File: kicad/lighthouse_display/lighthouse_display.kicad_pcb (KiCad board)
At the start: 2 copper layers, 0 parts

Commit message: sch: all leds connected, also set all footprints
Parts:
- added C1: 100nF, Capacitor_SMD:C_0603_1608Metric_Pad1.08x0.95mm_HandSolder, F.Cu at (237.0, 76.7)
- added C11: 1uF, Capacitor_SMD:C_0805_2012Metric_Pad1.18x1.45mm_HandSolder, F.Cu at (250.3, 89.0)
- added C2: 10uF, Capacitor_SMD:C_0805_2012Metric_Pad1.18x1.45mm_HandSolder, F.Cu at (250.3, 77.0)
- added C3: 470nF, Capacitor_SMD:C_0603_1608Metric_Pad1.08x0.95mm_HandSolder, F.Cu at (237.0, 79.2)
- added C4: 1uF, Capacitor_SMD:C_0805_2012Metric_Pad1.18x1.45mm_HandSolder, F.Cu at (250.3, 80.0)
- added C5: 10uF, Capacitor_SMD:C_0805_2012Metric_Pad1.18x1.45mm_HandSolder, F.Cu at (250.3, 83.0)
- added C6: 100nF, Capacitor_SMD:C_0603_1608Metric_Pad1.08x0.95mm_HandSolder, F.Cu at (237.0, 81.7)
- added C7: 10uF, Capacitor_SMD:C_0805_2012Metric_Pad1.18x1.45mm_HandSolder, F.Cu at (250.3, 86.0)
- added C8: 100nF, Capacitor_SMD:C_0603_1608Metric_Pad1.08x0.95mm_HandSolder, F.Cu at (237.0, 84.2)
- added D1: 1206MIL, LED_SMD:LED_1206_3216Metric_Pad1.42x1.75mm_HandSolder, F.Cu at (189.7, 77.1)
- added D10: 1206MIL, LED_SMD:LED_1206_3216Metric_Pad1.42x1.75mm_HandSolder, F.Cu at (189.7, 107.7)
- added D100: PMEG4010CEJ, Diode_SMD:D_SOD-323F, F.Cu at (254.8, 82.2)
- added D11: 1206MIL, LED_SMD:LED_1206_3216Metric_Pad1.42x1.75mm_HandSolder, F.Cu at (189.7, 111.1)
- added D12: 1206MIL, LED_SMD:LED_1206_3216Metric_Pad1.42x1.75mm_HandSolder, F.Cu at (189.7, 114.5)
- added D13: 1206MIL, LED_SMD:LED_1206_3216Metric_Pad1.42x1.75mm_HandSolder, F.Cu at (189.7, 117.8)
- added D14: 1206MIL, LED_SMD:LED_1206_3216Metric_Pad1.42x1.75mm_HandSolder, F.Cu at (189.7, 121.2)
- added D15: 1206MIL, LED_SMD:LED_1206_3216Metric_Pad1.42x1.75mm_HandSolder, F.Cu at (189.7, 124.6)
- added D16: 1206MIL, LED_SMD:LED_1206_3216Metric_Pad1.42x1.75mm_HandSolder, F.Cu at (195.7, 77.2)
- added D17: 1206MIL, LED_SMD:LED_1206_3216Metric_Pad1.42x1.75mm_HandSolder, F.Cu at (195.7, 80.5)
- added D18: 1206MIL, LED_SMD:LED_1206_3216Metric_Pad1.42x1.75mm_HandSolder, F.Cu at (195.7, 83.9)
- added D19: 1206MIL, LED_SMD:LED_1206_3216Metric_Pad1.42x1.75mm_HandSolder, F.Cu at (195.7, 87.3)
- added D2: 1206MIL, LED_SMD:LED_1206_3216Metric_Pad1.42x1.75mm_HandSolder, F.Cu at (189.7, 80.5)
- added D20: 1206MIL, LED_SMD:LED_1206_3216Metric_Pad1.42x1.75mm_HandSolder, F.Cu at (195.7, 90.7)
- added D21: 1206MIL, LED_SMD:LED_1206_3216Metric_Pad1.42x1.75mm_HandSolder, F.Cu at (195.7, 94.1)
- added D22: 1206MIL, LED_SMD:LED_1206_3216Metric_Pad1.42x1.75mm_HandSolder, F.Cu at (195.7, 97.5)
- added D23: 1206MIL, LED_SMD:LED_1206_3216Metric_Pad1.42x1.75mm_HandSolder, F.Cu at (195.7, 100.9)
- added D24: 1206MIL, LED_SMD:LED_1206_3216Metric_Pad1.42x1.75mm_HandSolder, F.Cu at (195.7, 104.3)
- added D25: 1206MIL, LED_SMD:LED_1206_3216Metric_Pad1.42x1.75mm_HandSolder, F.Cu at (195.7, 107.7)
- added D26: 1206MIL, LED_SMD:LED_1206_3216Metric_Pad1.42x1.75mm_HandSolder, F.Cu at (195.7, 111.1)
- added D27: 1206MIL, LED_SMD:LED_1206_3216Metric_Pad1.42x1.75mm_HandSolder, F.Cu at (195.7, 114.5)
- added D28: 1206MIL, LED_SMD:LED_1206_3216Metric_Pad1.42x1.75mm_HandSolder, F.Cu at (195.7, 117.8)
- added D29: 1206MIL, LED_SMD:LED_1206_3216Metric_Pad1.42x1.75mm_HandSolder, F.Cu at (195.7, 121.2)
- added D3: 1206MIL, LED_SMD:LED_1206_3216Metric_Pad1.42x1.75mm_HandSolder, F.Cu at (189.7, 83.9)
- added D30: 1206MIL, LED_SMD:LED_1206_3216Metric_Pad1.42x1.75mm_HandSolder, F.Cu at (195.7, 124.6)
- added D31: 1206MIL, LED_SMD:LED_1206_3216Metric_Pad1.42x1.75mm_HandSolder, F.Cu at (201.7, 77.2)
- added D32: 1206MIL, LED_SMD:LED_1206_3216Metric_Pad1.42x1.75mm_HandSolder, F.Cu at (201.7, 80.5)
- added D33: 1206MIL, LED_SMD:LED_1206_3216Metric_Pad1.42x1.75mm_HandSolder, F.Cu at (201.7, 83.9)
- added D34: 1206MIL, LED_SMD:LED_1206_3216Metric_Pad1.42x1.75mm_HandSolder, F.Cu at (201.7, 87.3)
- added D35: 1206MIL, LED_SMD:LED_1206_3216Metric_Pad1.42x1.75mm_HandSolder, F.Cu at (201.7, 90.7)
- added D36: 1206MIL, LED_SMD:LED_1206_3216Metric_Pad1.42x1.75mm_HandSolder, F.Cu at (201.7, 94.1)
- added D37: 1206MIL, LED_SMD:LED_1206_3216Metric_Pad1.42x1.75mm_HandSolder, F.Cu at (201.7, 97.5)
- added D38: 1206MIL, LED_SMD:LED_1206_3216Metric_Pad1.42x1.75mm_HandSolder, F.Cu at (201.7, 100.9)
- added D39: 1206MIL, LED_SMD:LED_1206_3216Metric_Pad1.42x1.75mm_HandSolder, F.Cu at (201.7, 104.3)
- added D4: 1206MIL, LED_SMD:LED_1206_3216Metric_Pad1.42x1.75mm_HandSolder, F.Cu at (189.7, 87.3)
- added D40: 1206MIL, LED_SMD:LED_1206_3216Metric_Pad1.42x1.75mm_HandSolder, F.Cu at (201.7, 107.7)
- added D41: 1206MIL, LED_SMD:LED_1206_3216Metric_Pad1.42x1.75mm_HandSolder, F.Cu at (201.7, 111.1)
- added D42: 1206MIL, LED_SMD:LED_1206_3216Metric_Pad1.42x1.75mm_HandSolder, F.Cu at (201.7, 114.5)
- added D43: 1206MIL, LED_SMD:LED_1206_3216Metric_Pad1.42x1.75mm_HandSolder, F.Cu at (201.7, 117.8)
- added D44: 1206MIL, LED_SMD:LED_1206_3216Metric_Pad1.42x1.75mm_HandSolder, F.Cu at (201.7, 121.2)
- added D45: 1206MIL, LED_SMD:LED_1206_3216Metric_Pad1.42x1.75mm_HandSolder, F.Cu at (201.7, 124.6)
- added D46: 1206MIL, LED_SMD:LED_1206_3216Metric_Pad1.42x1.75mm_HandSolder, F.Cu at (207.7, 77.2)
- added D47: 1206MIL, LED_SMD:LED_1206_3216Metric_Pad1.42x1.75mm_HandSolder, F.Cu at (207.7, 80.5)
- added D48: 1206MIL, LED_SMD:LED_1206_3216Metric_Pad1.42x1.75mm_HandSolder, F.Cu at (207.7, 83.9)
- added D49: 1206MIL, LED_SMD:LED_1206_3216Metric_Pad1.42x1.75mm_HandSolder, F.Cu at (207.7, 87.3)
- added D5: 1206MIL, LED_SMD:LED_1206_3216Metric_Pad1.42x1.75mm_HandSolder, F.Cu at (189.7, 90.7)
- added D50: 1206MIL, LED_SMD:LED_1206_3216Metric_Pad1.42x1.75mm_HandSolder, F.Cu at (207.7, 90.7)
- added D51: 1206MIL, LED_SMD:LED_1206_3216Metric_Pad1.42x1.75mm_HandSolder, F.Cu at (207.7, 94.1)
- added D52: 1206MIL, LED_SMD:LED_1206_3216Metric_Pad1.42x1.75mm_HandSolder, F.Cu at (207.7, 97.5)
- added D53: 1206MIL, LED_SMD:LED_1206_3216Metric_Pad1.42x1.75mm_HandSolder, F.Cu at (207.7, 100.9)
- added D54: 1206MIL, LED_SMD:LED_1206_3216Metric_Pad1.42x1.75mm_HandSolder, F.Cu at (207.7, 104.3)
- added D55: 1206MIL, LED_SMD:LED_1206_3216Metric_Pad1.42x1.75mm_HandSolder, F.Cu at (207.7, 107.7)
- added D56: 1206MIL, LED_SMD:LED_1206_3216Metric_Pad1.42x1.75mm_HandSolder, F.Cu at (207.7, 111.1)
- added D57: 1206MIL, LED_SMD:LED_1206_3216Metric_Pad1.42x1.75mm_HandSolder, F.Cu at (207.7, 114.5)
- added D58: 1206MIL, LED_SMD:LED_1206_3216Metric_Pad1.42x1.75mm_HandSolder, F.Cu at (207.7, 117.8)
- added D59: 1206MIL, LED_SMD:LED_1206_3216Metric_Pad1.42x1.75mm_HandSolder, F.Cu at (207.7, 121.2)
- added D6: 1206MIL, LED_SMD:LED_1206_3216Metric_Pad1.42x1.75mm_HandSolder, F.Cu at (189.7, 94.1)
- added D60: 1206MIL, LED_SMD:LED_1206_3216Metric_Pad1.42x1.75mm_HandSolder, F.Cu at (207.7, 124.6)
- added D61: 1206MIL, LED_SMD:LED_1206_3216Metric_Pad1.42x1.75mm_HandSolder, F.Cu at (213.7, 77.2)
- added D62: 1206MIL, LED_SMD:LED_1206_3216Metric_Pad1.42x1.75mm_HandSolder, F.Cu at (213.7, 80.5)
- added D63: 1206MIL, LED_SMD:LED_1206_3216Metric_Pad1.42x1.75mm_HandSolder, F.Cu at (213.7, 83.9)
- added D64: 1206MIL, LED_SMD:LED_1206_3216Metric_Pad1.42x1.75mm_HandSolder, F.Cu at (213.7, 87.3)
- added D65: 1206MIL, LED_SMD:LED_1206_3216Metric_Pad1.42x1.75mm_HandSolder, F.Cu at (213.7, 90.7)
- added D66: 1206MIL, LED_SMD:LED_1206_3216Metric_Pad1.42x1.75mm_HandSolder, F.Cu at (213.7, 94.1)
- added D67: 1206MIL, LED_SMD:LED_1206_3216Metric_Pad1.42x1.75mm_HandSolder, F.Cu at (213.7, 97.5)
- added D68: 1206MIL, LED_SMD:LED_1206_3216Metric_Pad1.42x1.75mm_HandSolder, F.Cu at (213.7, 100.9)
- added D69: 1206MIL, LED_SMD:LED_1206_3216Metric_Pad1.42x1.75mm_HandSolder, F.Cu at (213.7, 104.3)
- added D7: 1206MIL, LED_SMD:LED_1206_3216Metric_Pad1.42x1.75mm_HandSolder, F.Cu at (189.7, 97.5)
- added D70: 1206MIL, LED_SMD:LED_1206_3216Metric_Pad1.42x1.75mm_HandSolder, F.Cu at (213.7, 107.7)
- added D71: 1206MIL, LED_SMD:LED_1206_3216Metric_Pad1.42x1.75mm_HandSolder, F.Cu at (213.7, 111.1)
- added D72: 1206MIL, LED_SMD:LED_1206_3216Metric_Pad1.42x1.75mm_HandSolder, F.Cu at (213.7, 114.5)
- added D73: 1206MIL, LED_SMD:LED_1206_3216Metric_Pad1.42x1.75mm_HandSolder, F.Cu at (213.7, 117.8)
- added D74: 1206MIL, LED_SMD:LED_1206_3216Metric_Pad1.42x1.75mm_HandSolder, F.Cu at (213.7, 121.2)
- added D75: 1206MIL, LED_SMD:LED_1206_3216Metric_Pad1.42x1.75mm_HandSolder, F.Cu at (213.7, 124.6)
- added D76: 1206MIL, LED_SMD:LED_1206_3216Metric_Pad1.42x1.75mm_HandSolder, F.Cu at (219.7, 77.2)
- added D77: 1206MIL, LED_SMD:LED_1206_3216Metric_Pad1.42x1.75mm_HandSolder, F.Cu at (219.7, 80.5)
- added D78: 1206MIL, LED_SMD:LED_1206_3216Metric_Pad1.42x1.75mm_HandSolder, F.Cu at (219.7, 83.9)
- added D79: 1206MIL, LED_SMD:LED_1206_3216Metric_Pad1.42x1.75mm_HandSolder, F.Cu at (219.7, 87.3)
- added D8: 1206MIL, LED_SMD:LED_1206_3216Metric_Pad1.42x1.75mm_HandSolder, F.Cu at (189.7, 100.9)
- added D80: 1206MIL, LED_SMD:LED_1206_3216Metric_Pad1.42x1.75mm_HandSolder, F.Cu at (219.7, 90.7)
- added D81: 1206MIL, LED_SMD:LED_1206_3216Metric_Pad1.42x1.75mm_HandSolder, F.Cu at (219.7, 94.1)
- added D82: 1206MIL, LED_SMD:LED_1206_3216Metric_Pad1.42x1.75mm_HandSolder, F.Cu at (219.7, 97.5)
- added D83: 1206MIL, LED_SMD:LED_1206_3216Metric_Pad1.42x1.75mm_HandSolder, F.Cu at (219.7, 100.9)
- added D84: 1206MIL, LED_SMD:LED_1206_3216Metric_Pad1.42x1.75mm_HandSolder, F.Cu at (219.7, 104.3)
- added D85: 1206MIL, LED_SMD:LED_1206_3216Metric_Pad1.42x1.75mm_HandSolder, F.Cu at (219.7, 107.7)
- added D86: 1206MIL, LED_SMD:LED_1206_3216Metric_Pad1.42x1.75mm_HandSolder, F.Cu at (219.7, 111.1)
- added D87: 1206MIL, LED_SMD:LED_1206_3216Metric_Pad1.42x1.75mm_HandSolder, F.Cu at (219.7, 114.5)
- added D88: 1206MIL, LED_SMD:LED_1206_3216Metric_Pad1.42x1.75mm_HandSolder, F.Cu at (219.7, 117.8)
- added D89: 1206MIL, LED_SMD:LED_1206_3216Metric_Pad1.42x1.75mm_HandSolder, F.Cu at (219.7, 121.2)
- added D9: 1206MIL, LED_SMD:LED_1206_3216Metric_Pad1.42x1.75mm_HandSolder, F.Cu at (189.7, 104.3)
- added D90: 1206MIL, LED_SMD:LED_1206_3216Metric_Pad1.42x1.75mm_HandSolder, F.Cu at (219.7, 124.6)
- added D91: 1206MIL, LED_SMD:LED_1206_3216Metric_Pad1.42x1.75mm_HandSolder, F.Cu at (225.7, 77.2)
- added D92: 1206MIL, LED_SMD:LED_1206_3216Metric_Pad1.42x1.75mm_HandSolder, F.Cu at (225.7, 80.5)
- added D93: 1206MIL, LED_SMD:LED_1206_3216Metric_Pad1.42x1.75mm_HandSolder, F.Cu at (225.7, 83.9)
- added D94: 1206MIL, LED_SMD:LED_1206_3216Metric_Pad1.42x1.75mm_HandSolder, F.Cu at (225.7, 87.3)
- added D95: 1206MIL, LED_SMD:LED_1206_3216Metric_Pad1.42x1.75mm_HandSolder, F.Cu at (225.7, 90.7)
- added D96: 1206MIL, LED_SMD:LED_1206_3216Metric_Pad1.42x1.75mm_HandSolder, F.Cu at (225.7, 94.1)
- added D97: 1206MIL, LED_SMD:LED_1206_3216Metric_Pad1.42x1.75mm_HandSolder, F.Cu at (225.7, 97.5)
- added D98: 1206MIL, LED_SMD:LED_1206_3216Metric_Pad1.42x1.75mm_HandSolder, F.Cu at (225.7, 100.9)
- added D99: 1206MIL, LED_SMD:LED_1206_3216Metric_Pad1.42x1.75mm_HandSolder, F.Cu at (225.7, 104.3)
- added J1: Conn_01x12_Pin, Connector_PinHeader_1.27mm:PinHeader_1x12_P1.27mm_Vertical, F.Cu at (232.7, 77.1)
- added L1: 4.7uH, Inductor_SMD:L_Taiyo-Yuden_NR-60xx_HandSoldering, F.Cu at (250.1, 94.3)
- added R1: 1M3, Resistor_SMD:R_0603_1608Metric_Pad0.98x0.95mm_HandSolder, F.Cu at (237.0, 86.8)
- added R10: 1M, Resistor_SMD:R_0603_1608Metric_Pad0.98x0.95mm_HandSolder, F.Cu at (245.7, 79.2)
- added R11: 1M, Resistor_SMD:R_0603_1608Metric_Pad0.98x0.95mm_HandSolder, F.Cu at (245.7, 81.7)
- added R12: 20k, Resistor_SMD:R_0603_1608Metric_Pad0.98x0.95mm_HandSolder, F.Cu at (245.7, 84.2)
- added R2: 51k, Resistor_SMD:R_0603_1608Metric_Pad0.98x0.95mm_HandSolder, F.Cu at (237.0, 89.3)
- added R3: 1M, Resistor_SMD:R_0603_1608Metric_Pad0.98x0.95mm_HandSolder, F.Cu at (241.3, 76.7)
- added R4: 83k3, Resistor_SMD:R_0603_1608Metric_Pad0.98x0.95mm_HandSolder, F.Cu at (241.3, 79.2)
- added R5: 1M, Resistor_SMD:R_0603_1608Metric_Pad0.98x0.95mm_HandSolder, F.Cu at (241.3, 81.7)
- added R6: 4k7, Resistor_SMD:R_0603_1608Metric_Pad0.98x0.95mm_HandSolder, F.Cu at (241.3, 84.2)
- added R7: 4k7, Resistor_SMD:R_0603_1608Metric_Pad0.98x0.95mm_HandSolder, F.Cu at (241.3, 86.8)
- added R8: 1M, Resistor_SMD:R_0603_1608Metric_Pad0.98x0.95mm_HandSolder, F.Cu at (241.3, 89.3)
- added R9: 1M, Resistor_SMD:R_0603_1608Metric_Pad0.98x0.95mm_HandSolder, F.Cu at (245.7, 76.7)
- added U1: IS31FL3731-SA, Package_SO:SSOP-28_5.3x10.2mm_P0.65mm, F.Cu at (240.1, 96.5)
- added U2: TPS61176RTER, Package_DFN_QFN:Texas_RTE0016D_WQFN-16-1EP_3x3mm_P0.5mm_EP0.8x0.8mm, F.Cu at (255.3, 78.1)

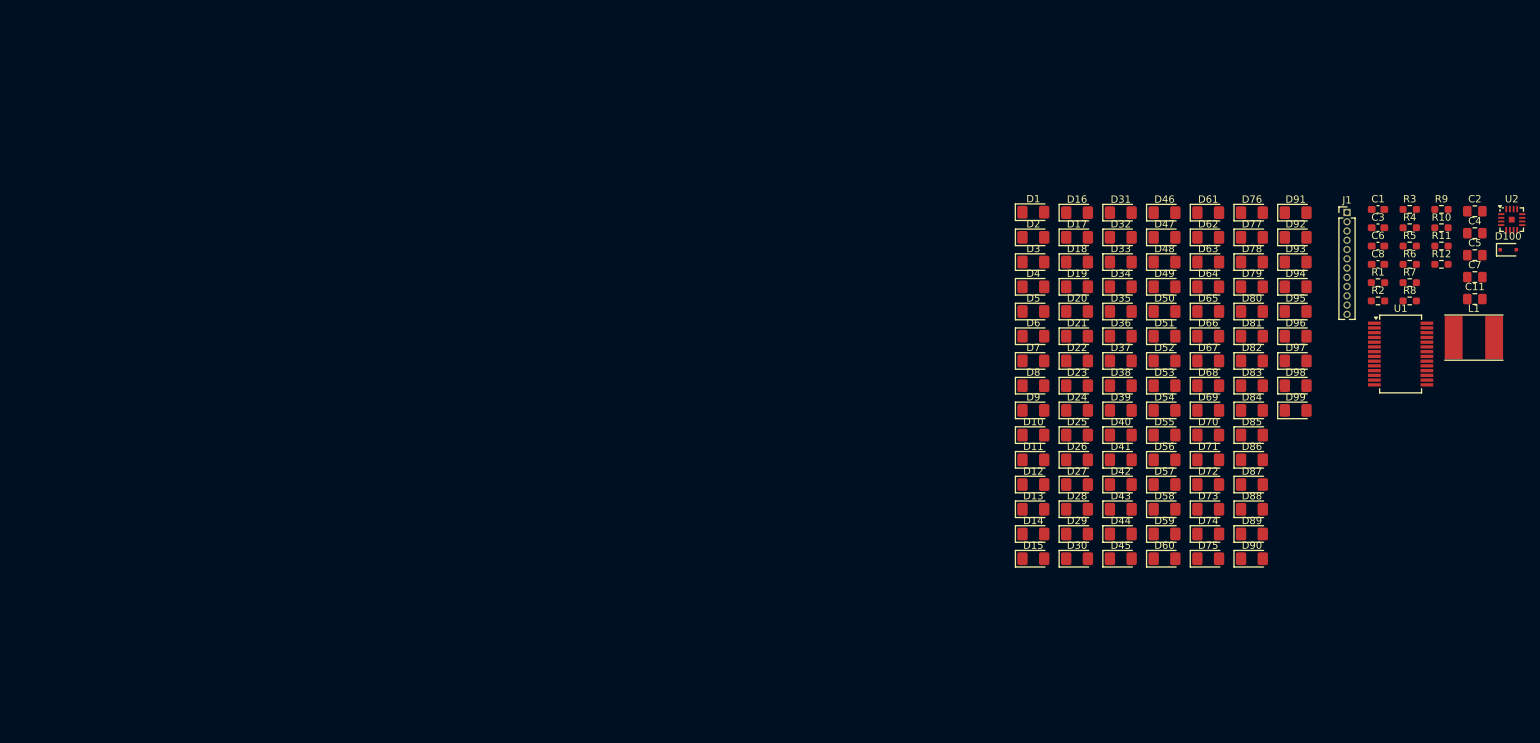
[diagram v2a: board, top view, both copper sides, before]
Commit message: hw display placed red and white leds
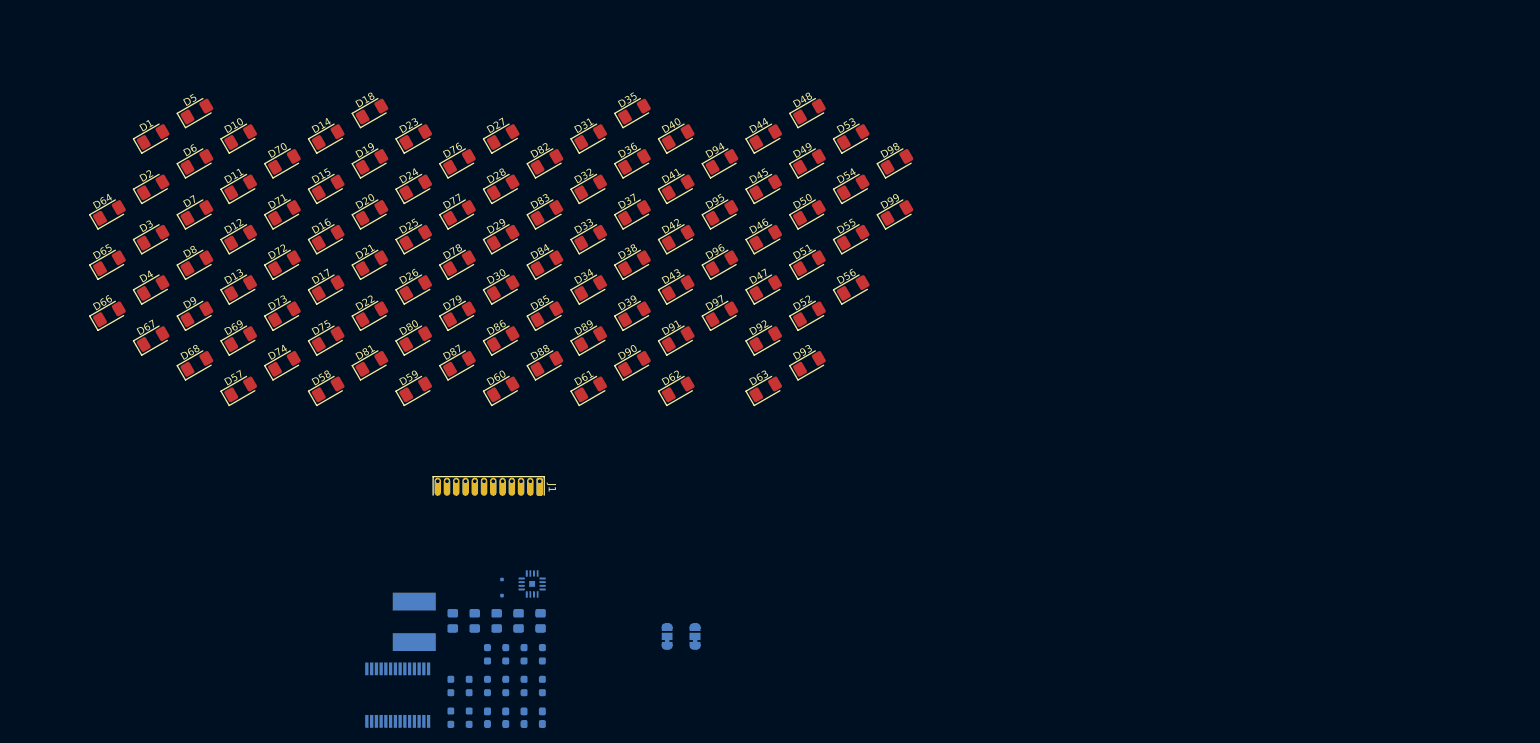
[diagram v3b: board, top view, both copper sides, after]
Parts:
- added JP1: Jumper_3_Bridged12, Jumper:SolderJumper-3_P1.3mm_Bridged12_RoundedPad1.0x1.5mm, B.Cu at (143.3, 135.3)
- added JP2: Jumper_3_Bridged12, Jumper:SolderJumper-3_P1.3mm_Bridged12_RoundedPad1.0x1.5mm, B.Cu at (139.5, 135.3)
- C1, C11, C2, C3, C4, C5, C6, C7, C8, D100, L1, R1, R10, R11, R12, R2, R3, R4, R5, R6, R7, R8, R9, U1, U2: moved to B.Cu
- J1: footprint Connector_PinHeader_1.27mm:PinHeader_1x12_P1.27mm_Vertical -> lighthouse:con_1x12_1.27mm_long_pads
- moved D64 151.0 mm to (63.0, 77.2), turned to 30 degrees
- moved D65 150.8 mm to (63.0, 84.1), turned to 30 degrees
- moved D66 150.7 mm to (63.0, 91.1), turned to 30 degrees
- moved L1 150.5 mm to (104.8, 133.3), turned to 90 degrees
- moved C11 146.9 mm to (110.1, 133.1), turned to 90 degrees
- moved D100 145.5 mm to (116.8, 128.6), turned to 90 degrees
- moved U1 145.3 mm to (102.5, 143.3), turned to 90 degrees
- moved C7 145.0 mm to (113.1, 133.1), turned to 90 degrees
- moved D67 144.7 mm to (69.0, 94.5), turned to 30 degrees
- moved U2 143.3 mm to (121.0, 128.1), turned to 90 degrees
- moved C5 143.2 mm to (116.1, 133.1), turned to 90 degrees
- moved R8 141.7 mm to (109.8, 142.1), turned to 90 degrees
- moved C4 141.5 mm to (119.1, 133.1), turned to 90 degrees
- moved R12 141.3 mm to (114.8, 137.7), turned to 90 degrees
- moved R7 140.3 mm to (112.3, 142.1), turned to 90 degrees
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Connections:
- C1 pad 1: +BATT -> +12V
- C11 pad 1: +3.3V -> Net-(JP1-C)
- C2 pad 1: +BATT -> +12V
- C7 pad 1: +BATT -> Net-(JP2-C)
- C8 pad 1: +BATT -> Net-(JP2-C)
- J1 pad 1: +BATT -> +12V
- J1 pad 12: GND -> unconnected-(J1-Pin_12-Pad12)
- J1 pad 2: GND -> +5V
- L1 pad 1: +BATT -> +12V
- U1 pad 2: +BATT -> Net-(JP2-C)
- U2 pad 15: +3.3V -> Net-(JP1-C)

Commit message: places both led drivers, started routing
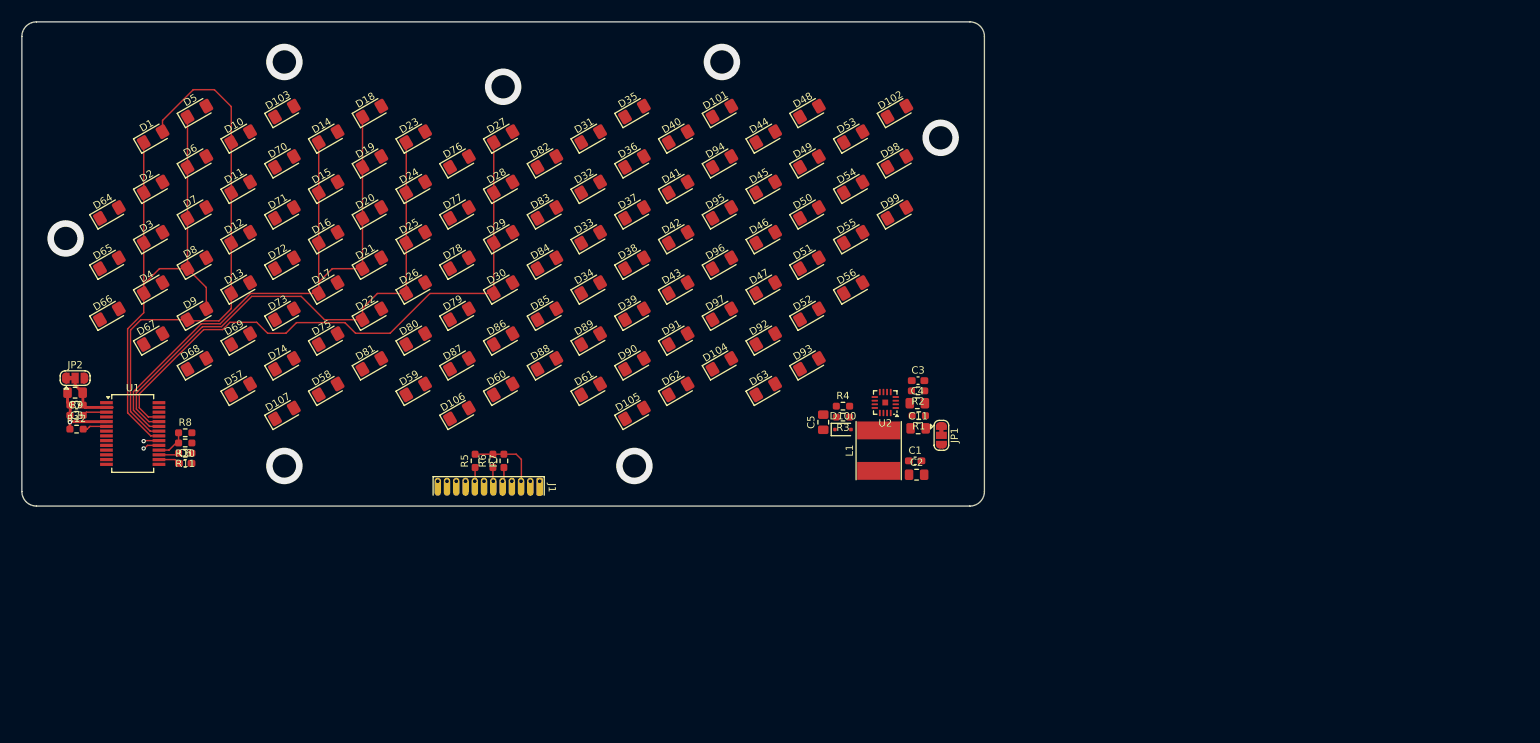
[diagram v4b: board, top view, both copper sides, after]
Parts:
- added D101: 1206MIL, LED_SMD:LED_1206_3216Metric_Pad1.42x1.75mm_HandSolder, F.Cu at (147.0, 63.3)
- added D102: 1206MIL, LED_SMD:LED_1206_3216Metric_Pad1.42x1.75mm_HandSolder, F.Cu at (171.0, 63.3)
- added D103: 1206MIL, LED_SMD:LED_1206_3216Metric_Pad1.42x1.75mm_HandSolder, F.Cu at (87.0, 63.3)
- added D104: 1206MIL, LED_SMD:LED_1206_3216Metric_Pad1.42x1.75mm_HandSolder, F.Cu at (147.0, 97.9)
- added D105: 1206MIL, LED_SMD:LED_1206_3216Metric_Pad1.42x1.75mm_HandSolder, F.Cu at (135.0, 104.7)
- added D106: 1206MIL, LED_SMD:LED_1206_3216Metric_Pad1.42x1.75mm_HandSolder, F.Cu at (111.0, 104.7)
- added D107: 1206MIL, LED_SMD:LED_1206_3216Metric_Pad1.42x1.75mm_HandSolder, F.Cu at (87.0, 104.7)
- C1, C11, C2, C3, C4, C5, C6, C7, C8, D100, JP1, JP2, L1, R1, R10, R11, R12, R2, R3, R4, R5, R6, R7, R8, R9, U1, U2: moved to F.Cu
- moved JP2 88.6 mm to (58.3, 99.8), turned to 0 degrees
- moved R2 78.2 mm to (173.9, 101.6), turned to 180 degrees
- moved R1 74.3 mm to (174.0, 105.0), turned to 180 degrees
- moved R9 71.8 mm to (58.5, 105.0), turned to 0 degrees
- moved C3 71.1 mm to (173.9, 100.2), turned to 0 degrees
- moved C8 70.8 mm to (58.5, 103.5), turned to 180 degrees
- moved C11 69.1 mm to (173.9, 106.7), turned to 0 degrees
- moved L1 67.9 mm to (168.5, 109.8)
- moved R12 64.3 mm to (58.5, 106.8), turned to 0 degrees
- moved C7 63.1 mm to (58.3, 101.8), turned to 180 degrees
- moved C4 62.3 mm to (173.8, 103.3), turned to 0 degrees
- moved C1 62.1 mm to (173.5, 111.2), turned to 0 degrees
- moved R4 58.2 mm to (163.6, 103.7), turned to 0 degrees
- moved C6 56.1 mm to (73.4, 111.5), turned to 0 degrees
- moved C2 55.3 mm to (173.7, 113.1), turned to 0 degrees
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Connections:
- net Net-(D100-A) renamed /TPS_SW
- net Net-(JP1-C) renamed /TPS_VIN
- net Net-(JP2-C) renamed /IS_VIN
- net Net-(U1-AD) renamed /IS_AD
- net Net-(U1-C_FILT) renamed /IS_FILT
- net Net-(U1-IN) renamed /IS_IN
- net Net-(U1-R_EXT) renamed /IS_REXT
- net Net-(U2-COMP) renamed /TPS_COMP
- net Net-(U2-ISET) renamed /TPS_ISET
- net Net-(U2-MODE/FAULT) renamed /TPS_MODE
- net Net-(U2-OVP) renamed /TPS_FB
- net Net-(U2-VLDO) renamed /TPS_LDO
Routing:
- net CA3: track 0.00 -> 86.2 mm
- net CA5: track 0.00 -> 82.6 mm
- net CA1: track 0.00 -> 77.9 mm
- net CA4: track 0.00 -> 73.0 mm
- net CA2: track 0.00 -> 72.7 mm
- net GND: track 0.00 -> 10.2 mm, vias 0 -> 1
- net +3.3V: track 0.00 -> 9.66 mm
- net /IS_VIN: track 0.00 -> 8.61 mm
- net /IS_AD: track 0.00 -> 4.49 mm
- net /SDA: track 0.00 -> 4.38 mm, vias 0 -> 1
- net /SCL: track 0.00 -> 4.04 mm, vias 0 -> 1
- net /~{SDB}: track 0.00 -> 3.36 mm
- net /IS_REXT: track 0.00 -> 3.34 mm
- net /IS_FILT: track 0.00 -> 2.95 mm
- net /IS_IN: track 0.00 -> 2.78 mm
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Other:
- board outline added: 132 x 66.4 mm

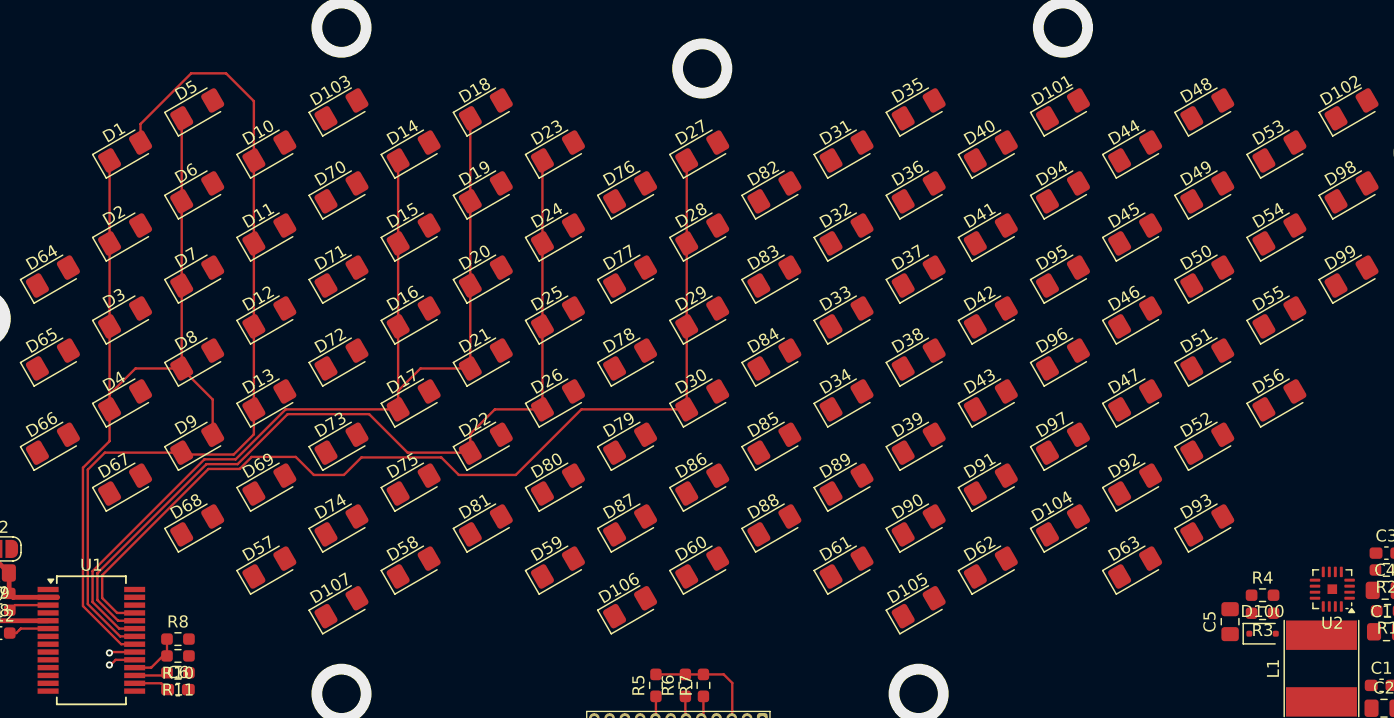
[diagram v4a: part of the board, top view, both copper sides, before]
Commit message: red leds routing, not done yet
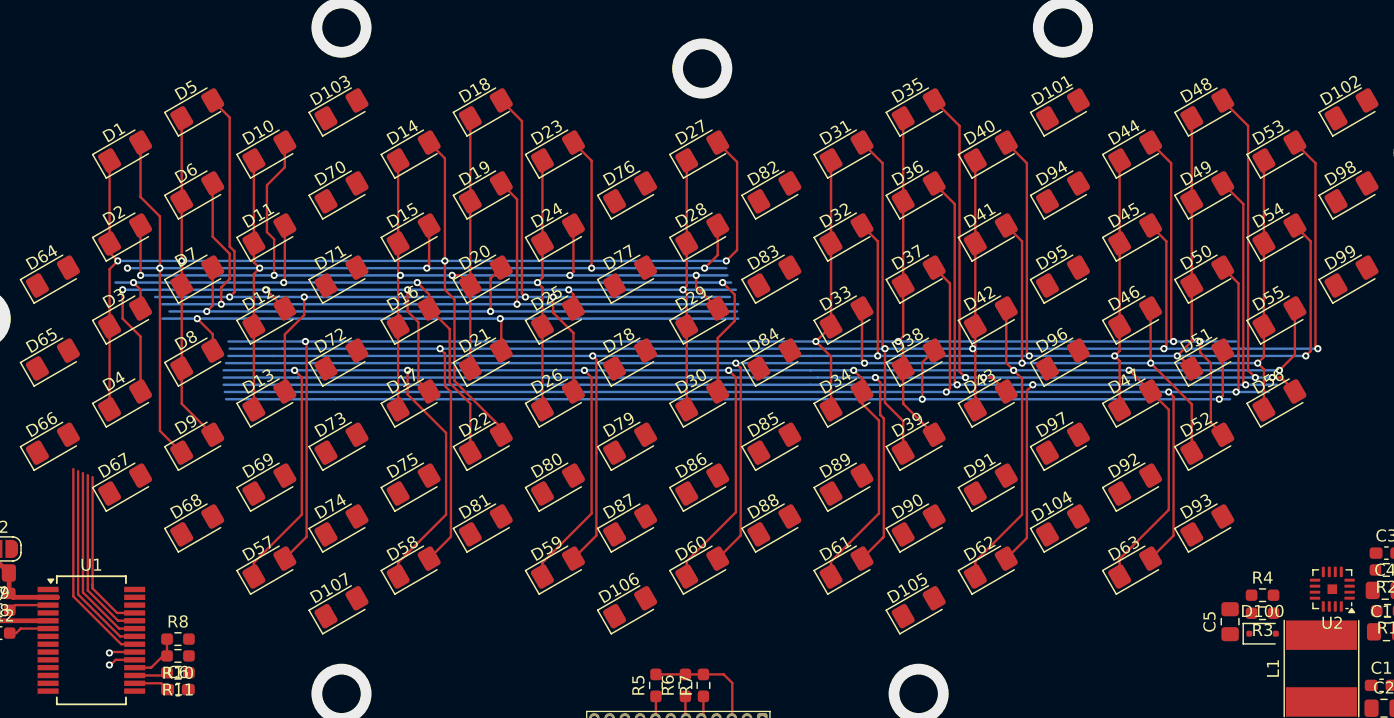
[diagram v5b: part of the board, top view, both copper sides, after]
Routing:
- net CB5: track 0.00 -> 235.1 mm, vias 0 -> 8
- net CB3: track 0.00 -> 191.8 mm, vias 0 -> 6
- net CB2: track 0.00 -> 186.0 mm, vias 0 -> 5
- net CB1: track 0.00 -> 178.0 mm, vias 0 -> 5
- net CB6: track 0.00 -> 156.3 mm, vias 0 -> 5
- net CB4: track 0.00 -> 154.2 mm, vias 0 -> 5
- net CB7: track 0.00 -> 138.0 mm, vias 0 -> 3
- net CB8: track 0.00 -> 123.6 mm, vias 0 -> 3
- net CA6: track 0.00 -> 99.3 mm, vias 0 -> 4
- net CB9: track 0.00 -> 92.1 mm, vias 0 -> 2
- net CA1: track 77.9 -> 154.4 mm, vias 0 -> 4
- net CA7: track 0.00 -> 69.4 mm, vias 0 -> 2
- net CA2: track 72.7 -> 133.9 mm, vias 0 -> 6
- net CA8: track 0.00 -> 55.1 mm, vias 0 -> 2
- net CA9: track 0.00 -> 53.8 mm, vias 0 -> 2
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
